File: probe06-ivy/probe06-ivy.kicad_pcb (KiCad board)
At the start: 2 copper layers, 80 x 80 mm, 106 parts, among them J1 USB_B_Micro, J2 Conn_Coaxial, Q1 S9014, SW1 SW_Push, SW2 SW_SPDT, U1 STM32F407VGTx, U2 MP1584EN, U3 AMS1117-3.3, U4 NEO-M8M, U5 XBP9B-DPST-001, U6 24LC32, U7 BMP280, Y1 8 MHz, Y2 32.768 KHz

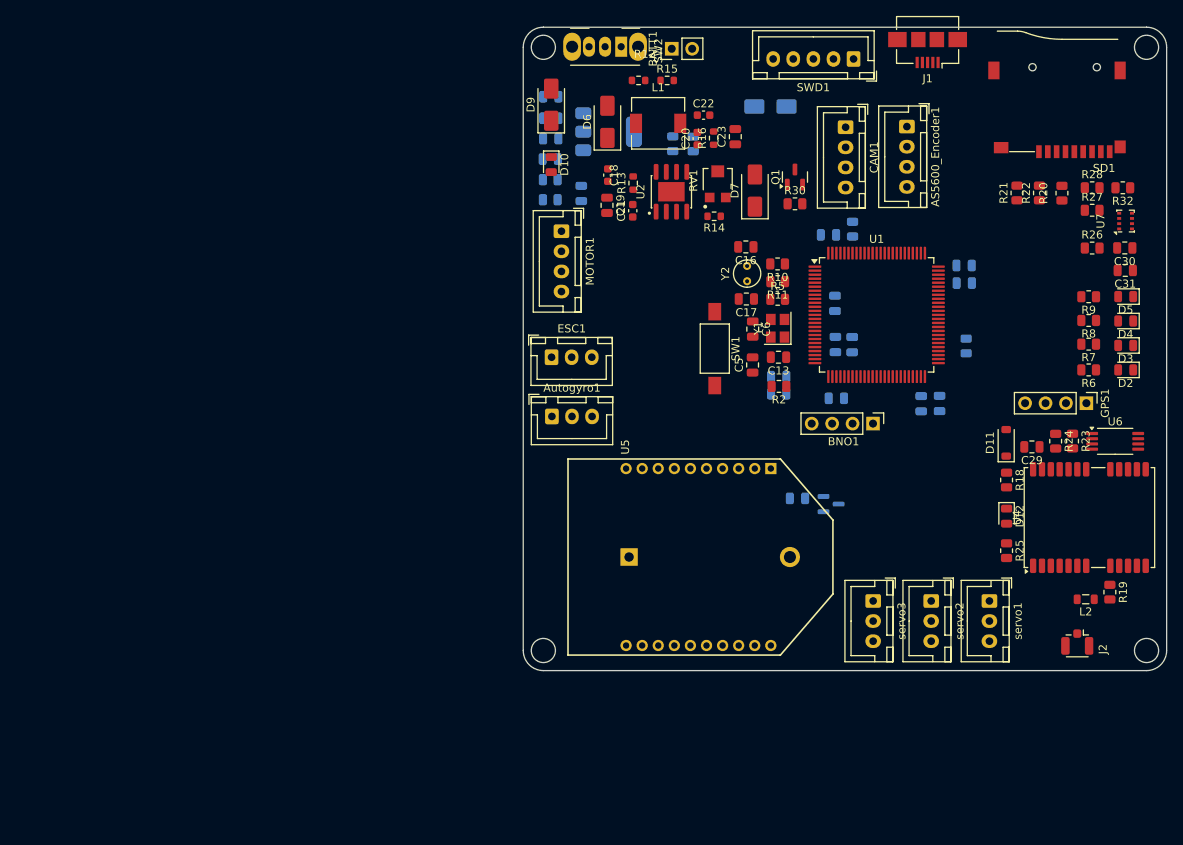
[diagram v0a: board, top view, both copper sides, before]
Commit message: route crystal and some bypass cap
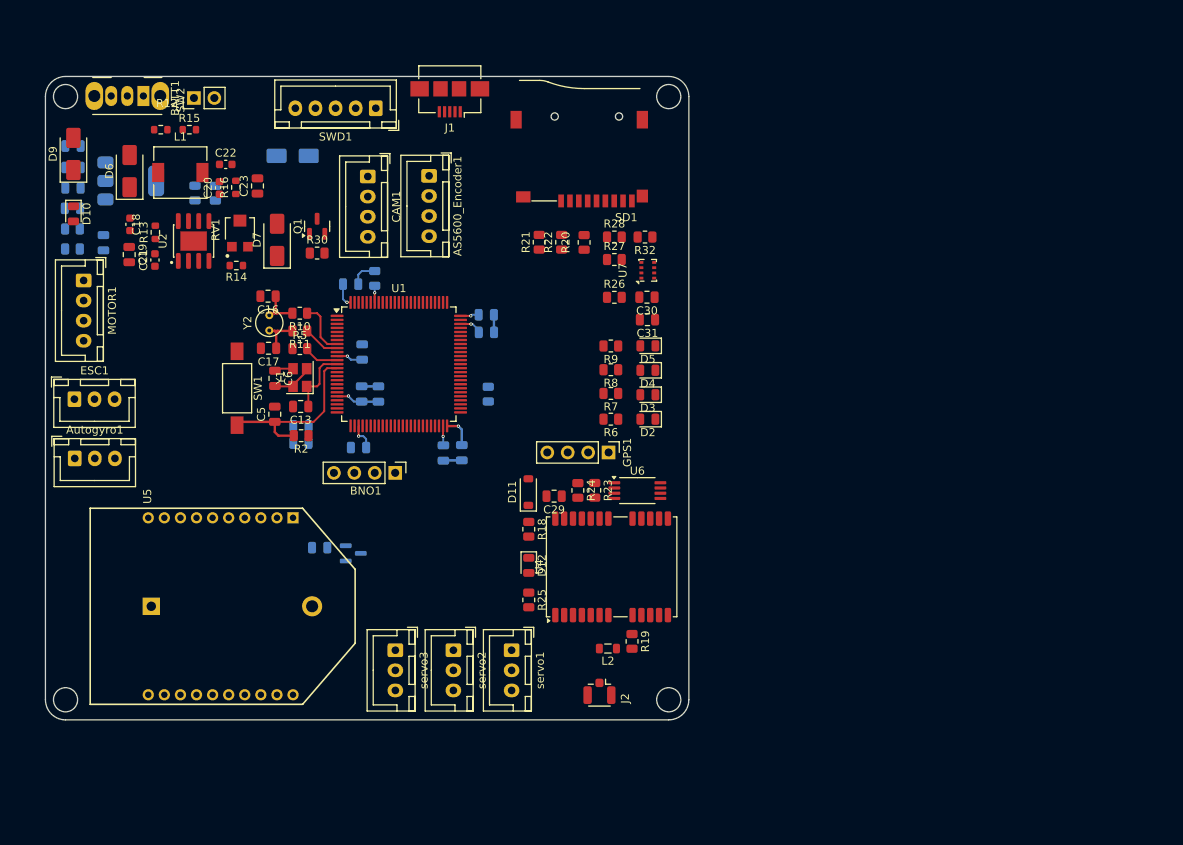
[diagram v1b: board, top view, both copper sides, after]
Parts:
- moved C10 59.7 mm to (141.5, 100.8)
- moved C11 59.7 mm to (157.4, 84.3)
- moved C24 59.7 mm to (136.7, 113.2)
- moved C3 59.7 mm to (134.4, 100.2)
- moved C30 59.7 mm to (177.4, 82.1)
- moved C4 59.7 mm to (134.4, 98.1)
- moved D2 59.7 mm to (177.5, 97.2)
- moved D3 59.7 mm to (177.5, 94.2)
- moved D5 59.7 mm to (177.5, 88.1)
- moved GPS1 59.7 mm to (172.6, 101.4)
- moved R13 59.7 mm to (116.3, 74.0)
- moved R24 59.7 mm to (168.8, 106.1)
- moved R26 59.7 mm to (173.3, 82.1)
- moved R27 59.7 mm to (173.3, 77.4)
- moved R6 59.7 mm to (172.9, 97.2)
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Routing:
- net Net-(U1-NRST): track 0.00 -> 22.4 mm
- net +3V3: track 0.00 -> 18.1 mm, vias 0 -> 5
- net GND: track 0.00 -> 17.3 mm
- net Net-(U1-PH1): track 0.00 -> 8.67 mm
- net Net-(U1-PC14): track 0.00 -> 6.81 mm
- net Net-(C16-Pad1): track 0.00 -> 5.50 mm
- net /VREF+: track 0.00 -> 5.47 mm, vias 0 -> 1
- net Net-(C17-Pad1): track 0.00 -> 5.43 mm
- net Net-(U1-PC15): track 0.00 -> 4.60 mm
- net Net-(U1-PH0): track 0.00 -> 4.44 mm
- net Net-(U1-VCAP_2): track 0.00 -> 2.85 mm, vias 0 -> 1
- net Net-(U1-VCAP_1): track 0.00 -> 2.44 mm, vias 0 -> 1
- net Net-(C6-Pad1): track 0.00 -> 2.35 mm
- net Net-(U1-BOOT0): track 0.00 -> 2.08 mm, vias 0 -> 1

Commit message: Routing (2) - make the pcb edge cuts to suit mechanic requirements - route some components (power, usb debug, gps) progress 50%
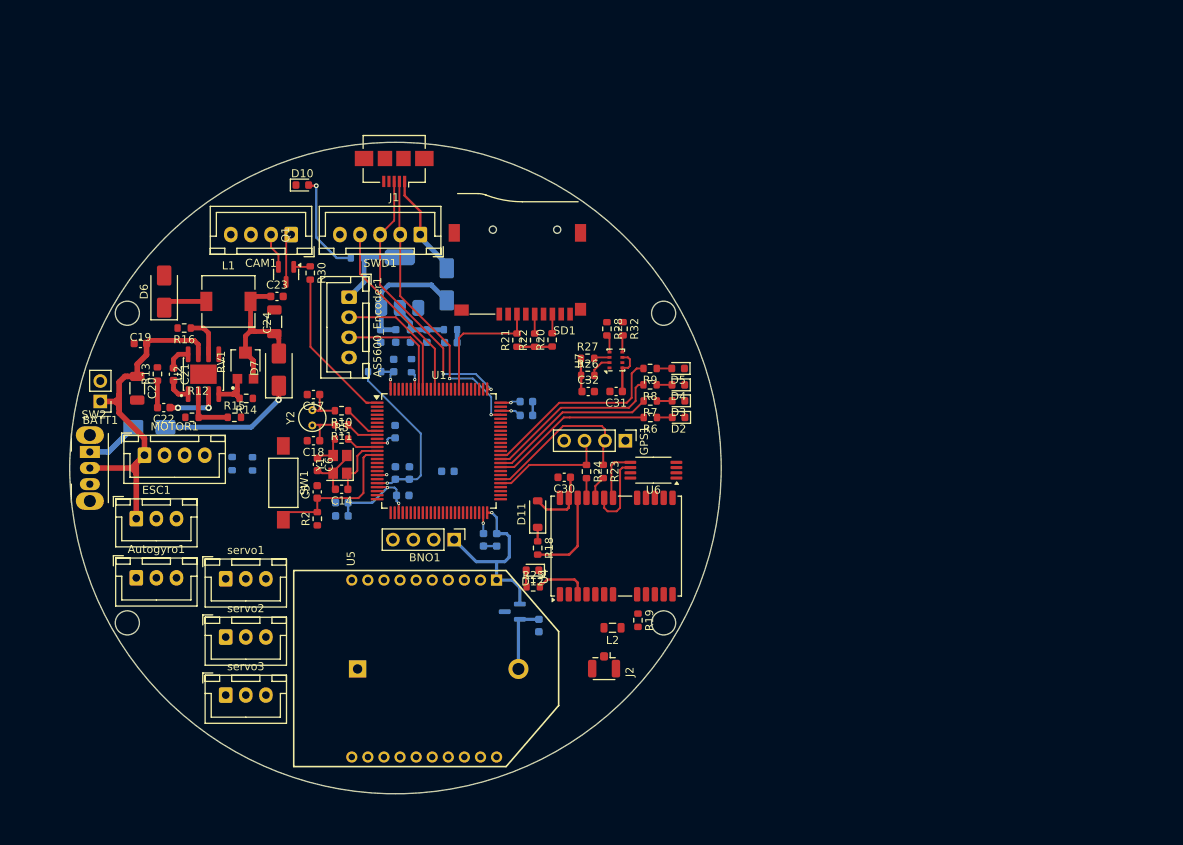
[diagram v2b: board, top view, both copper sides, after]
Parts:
- added C13: 100nF, Capacitor_SMD:C_0603_1608Metric, B.Cu at (153.0, 87.7)
- C1, C10, C11, C12, C2, C3, C4, C5, C6, C7, C8, C9: footprint Capacitor_SMD:C_0805_2012Metric -> Capacitor_SMD:C_0603_1608Metric
- C14: renamed from C13; footprint Capacitor_SMD:C_0805_2012Metric -> Capacitor_SMD:C_0603_1608Metric
- C15: renamed from C14; footprint Capacitor_SMD:C_0805_2012Metric -> Capacitor_SMD:C_0603_1608Metric
- C16: renamed from C15; footprint Capacitor_SMD:C_0805_2012Metric -> Capacitor_SMD:C_0603_1608Metric
- C17: renamed from C16; footprint Capacitor_SMD:C_0805_2012Metric -> Capacitor_SMD:C_0603_1608Metric
- C18: renamed from C17; footprint Capacitor_SMD:C_0805_2012Metric -> Capacitor_SMD:C_0603_1608Metric
- C20: renamed from C19; footprint Capacitor_SMD:C_0805_2012Metric -> Capacitor_SMD:C_1206_3216Metric
- C24: renamed from C23; footprint Capacitor_SMD:C_0805_2012Metric -> Capacitor_SMD:C_1206_3216Metric
- C25: renamed from C24; footprint Capacitor_SMD:C_0805_2012Metric -> Capacitor_SMD:C_0603_1608Metric
- C26: renamed from C25; footprint Capacitor_SMD:C_0805_2012Metric -> Capacitor_SMD:C_0603_1608Metric
- C27: renamed from C26; footprint Capacitor_SMD:C_0805_2012Metric -> Capacitor_SMD:C_0603_1608Metric
- C28: renamed from C27; footprint Capacitor_SMD:C_0805_2012Metric -> Capacitor_SMD:C_0603_1608Metric
- C29: renamed from C28; footprint Capacitor_SMD:C_0805_2012Metric -> Capacitor_SMD:C_0603_1608Metric
- C30: renamed from C29; footprint Capacitor_SMD:C_0805_2012Metric -> Capacitor_SMD:C_0603_1608Metric
- C31: renamed from C30; footprint Capacitor_SMD:C_0805_2012Metric -> Capacitor_SMD:C_0603_1608Metric
- C32: renamed from C31; footprint Capacitor_SMD:C_0805_2012Metric -> Capacitor_SMD:C_0603_1608Metric
- D10, D12, D2, D3, D4, D5: footprint LED_SMD:LED_0805_2012Metric -> LED_SMD:LED_0603_1608Metric
- D9: moved to B.Cu
- R1, R10, R11, R17, R18, R19, R2, R20, R21, R22, R23, R24, R25, R26, R27, R28, R29, R3, R30, R31, R32, R4, R5, R6, R7, R8, R9: footprint Resistor_SMD:R_0805_2012Metric -> Resistor_SMD:R_0603_1608Metric
- moved C12 51.4 mm to (152.6, 103.7), turned to 0 degrees
- moved R4 48.1 mm to (153.0, 86.1)
- moved C28 46.8 mm to (150.0, 86.9), turned to -90 degrees
- moved C29 45.8 mm to (148.0, 86.9), turned to -90 degrees
- moved C26 45.3 mm to (146.1, 86.9), turned to -90 degrees
- moved C27 45.0 mm to (144.3, 86.9), turned to -90 degrees
- moved SW2 44.8 mm to (108.1, 101.3), turned to -90 degrees
- moved BATT1 39.5 mm to (109.4, 95.0), turned to 180 degrees
- moved servo1 36.6 mm to (125.0, 117.1), turned to 0 degrees
- moved R15 36.2 mm to (126.1, 97.0)
- moved R12 36.0 mm to (120.8, 97.0)
- moved U3 35.8 mm to (146.7, 80.3), turned to 90 degrees
- moved R17 35.6 mm to (141.4, 77.2), turned to 180 degrees
- moved D9 35.3 mm to (115.5, 98.2), turned to 180 degrees
- moved R31 34.0 mm to (128.3, 102.8)
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- renumbered C18 to C19, C20 to C21, C21 to C22, C22 to C23
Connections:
- C12 pad 1: Net-(C12-Pad1) -> +3V3
- R4 pad 2: Net-(C12-Pad1) -> Net-(C13-Pad1)
- SWD1 pad 1: SWCLK -> +U5V
- SWD1 pad 3: SWO -> SWCLK
- SWD1 pad 4: +U5V -> SWO
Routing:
- net +3V3: track 18.1 -> 87.0 mm, vias 5 -> 7
- net +BATT: track 0.00 -> 46.2 mm
- net SWDIO: track 0.00 -> 36.6 mm, vias 0 -> 2
- net SWCLK: track 0.00 -> 35.9 mm, vias 0 -> 2
- net +5V: track 0.00 -> 33.2 mm, vias 0 -> 1
- net /LED4: track 0.00 -> 24.0 mm
- net SWO: track 0.00 -> 23.1 mm
- net /LED3: track 0.00 -> 22.5 mm
- net /LED2: track 0.00 -> 21.0 mm
- net Net-(D7-A): track 0.00 -> 20.5 mm
- net RX3: track 0.00 -> 20.4 mm
- net /LED1: track 0.00 -> 20.3 mm
- net +3V0: track 0.00 -> 20.0 mm
- net CAM: track 0.00 -> 19.5 mm
- net SDIO_CMD: track 0.00 -> 16.2 mm
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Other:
- board size 80 x 80 mm -> 81 x 81 mm

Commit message: Routing (3) Signal routing mostly done with something that needs TODO next: - Correction for power signals - Tidy up component silkscreen - Add team name and tagline
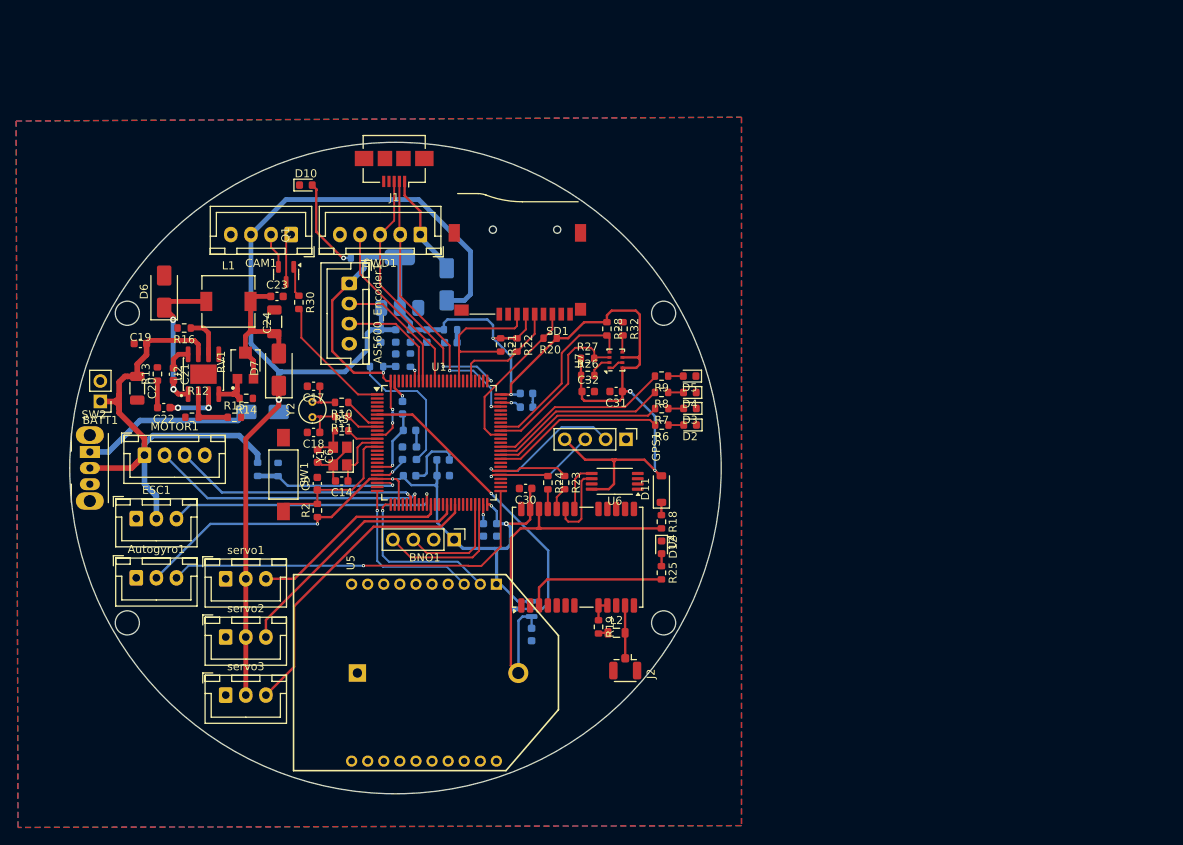
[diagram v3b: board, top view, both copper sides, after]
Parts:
- moved D12 16.3 mm to (179.2, 113.2), turned to -90 degrees
- moved R25 16.0 mm to (179.2, 116.3), turned to -90 degrees
- moved R18 15.7 mm to (179.2, 110.0)
- moved D11 15.7 mm to (179.2, 105.9)
- moved D9 14.2 mm to (129.6, 96.3)
- moved C4 13.0 mm to (152.1, 104.3), turned to 180 degrees
- moved C3 9.80 mm to (147.9, 104.3), turned to 180 degrees
- moved C12 6.97 mm to (147.9, 98.6)
- moved C10 6.68 mm to (152.0, 102.3)
- moved R23 5.00 mm to (167.1, 105.1)
- moved R24 5.00 mm to (165.1, 105.1)
- moved U4 5.00 mm to (168.8, 114.4)
- moved U6 5.00 mm to (173.4, 105.0)
- moved C30 5.00 mm to (162.3, 105.8)
- moved R19 4.97 mm to (171.4, 123.1)
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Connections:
- Autogyro1 pad 1: Autogyro -> GND
- Autogyro1 pad 3: GND -> Autogyro
- ESC1 pad 1: +BATT -> GND
- ESC1 pad 2: PWM1 -> +BATT
- ESC1 pad 3: GND -> PWM3
- MOTOR1 pad 2: PWM6 -> PWM2
- MOTOR1 pad 3: PWM5 -> PWM1
- U1 pad 18: Autogyro -> unconnected-(U1-PC3-Pad18)
- U1 pad 51: unconnected-(U1-PB12-Pad51) -> Autogyro
- servo1 pad 1: PWM2 -> GND
- servo1 pad 3: GND -> PWM4
- servo2 pad 1: PWM3 -> GND
- servo2 pad 3: GND -> PWM5
- servo3 pad 1: PWM4 -> GND
- servo3 pad 3: GND -> PWM6
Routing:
- net +3V3: track 87.0 -> 256.2 mm, vias 7 -> 12
- net +5V: track 33.2 -> 126.3 mm
- net Autogyro: track 0.00 -> 48.9 mm, vias 0 -> 1
- net /VBAT: track 0.00 -> 39.0 mm, vias 0 -> 1
- net PWM6: track 0.00 -> 38.4 mm
- net PWM2: track 0.00 -> 34.8 mm, vias 0 -> 1
- net PWM3: track 0.00 -> 34.3 mm, vias 0 -> 1
- net PWM5: track 0.00 -> 31.3 mm
- net PWM1: track 0.00 -> 31.2 mm, vias 0 -> 1
- net +3V0: track 20.0 -> 49.0 mm
- net PWM4: track 0.00 -> 25.0 mm
- net RX2: track 0.00 -> 20.8 mm, vias 0 -> 1
- net TX2: track 0.00 -> 20.7 mm, vias 0 -> 1
- net SCL3: track 2.21 -> 22.3 mm
- net VOLT: track 0.00 -> 19.3 mm, vias 0 -> 1
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- added copper zone on B.Cu, net GND
- added copper zone on F.Cu, net GND

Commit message: Routing (3)
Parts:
- added G***: LOGO, graphics:logobamantara, B.Cu at (164.0, 83.0)
- SD CARD: renamed from SD1
- U-BLOX: renamed from U4; value NEO-M8M -> U-BLOX
- moved C30 1.82 mm to (163.3, 104.4)
- moved D11 1.62 mm to (179.7, 104.4)
- moved D12 1.62 mm to (179.8, 111.6)
- moved J2 1.62 mm to (175.2, 126.5)
- moved R18 1.62 mm to (179.7, 108.5)
- moved R24 1.62 mm to (165.6, 103.6)
- moved R25 1.62 mm to (179.7, 114.8)
- moved U-BLOX 1.62 mm to (169.3, 112.9)
- moved U6 1.62 mm to (173.9, 103.4)
- moved R23 1.62 mm to (167.7, 103.6)
- moved R19 1.62 mm to (171.9, 121.5)
- moved L2 1.56 mm to (174.2, 122.3)
- moved D2 1.31 mm to (182.7, 99.3)
- moved R6 1.30 mm to (179.3, 99.3)
- moved D3 0.79 mm to (182.7, 96.7)
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- renumbered AS5600_Encoder1 to AS5600, Autogyro1 to Autogyro, U7 to BMP280, BNO1 to BNO055, GPS1 to GPS, SWD1 to SWD, U5 to XBEE
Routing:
- net GND: track 23.0 -> 33.5 mm, vias 1 -> 59
- net +BATT: track 64.8 -> 72.1 mm
- net +3V0: track 49.0 -> 44.4 mm
- net /VBAT: track 39.0 -> 35.0 mm
- net +3V3: track 256.2 -> 252.8 mm
- net Net-(D2-A): track 1.90 -> 0.00 mm
- net Net-(D3-A): track 1.90 -> 0.00 mm
- net TX3: track 21.0 -> 22.3 mm
- net Net-(U1-VCAP_1): track 3.44 -> 2.42 mm
- net Net-(D7-A): track 20.5 -> 19.7 mm
- net RX3: track 27.9 -> 28.7 mm
- net Net-(D6-K): track 19.4 -> 20.0 mm
- net /LED1: track 21.5 -> 22.1 mm
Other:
- board text added: "#3121 Bamantara EEPISAT"
- board text added: "#DOA_IBU #Bismillah_Juara_1"
- board text added: "+"
- board text added: "-"
- board text added: "CanSat Competition 2025 Auto Gyro Descender"
- board text added: "Garudaku Jaya Diangkasa"
- board text added: "RX"
- board text added: "S"
- board text added: "TX"

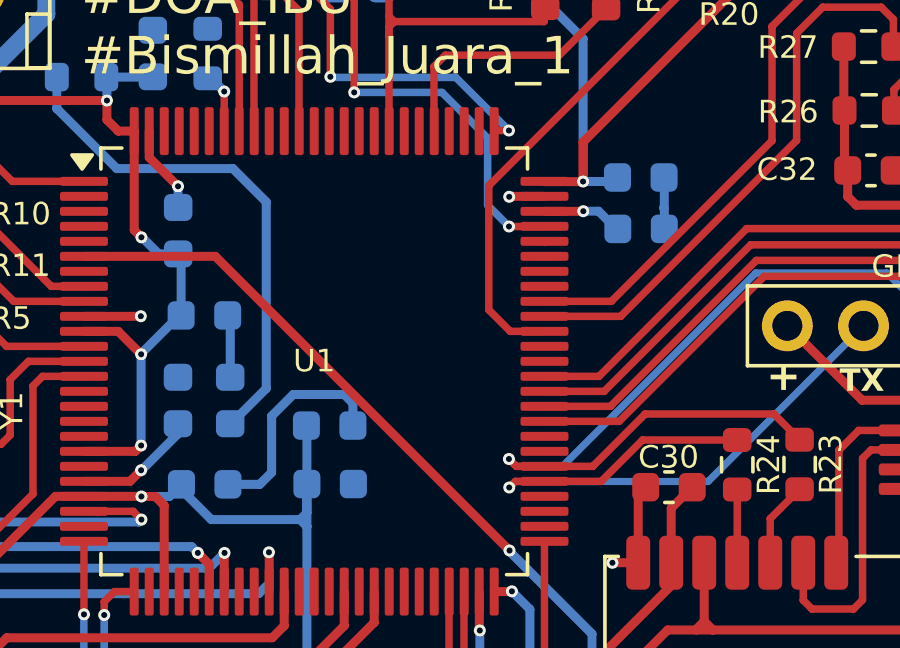
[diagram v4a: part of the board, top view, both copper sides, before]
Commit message: order id placement
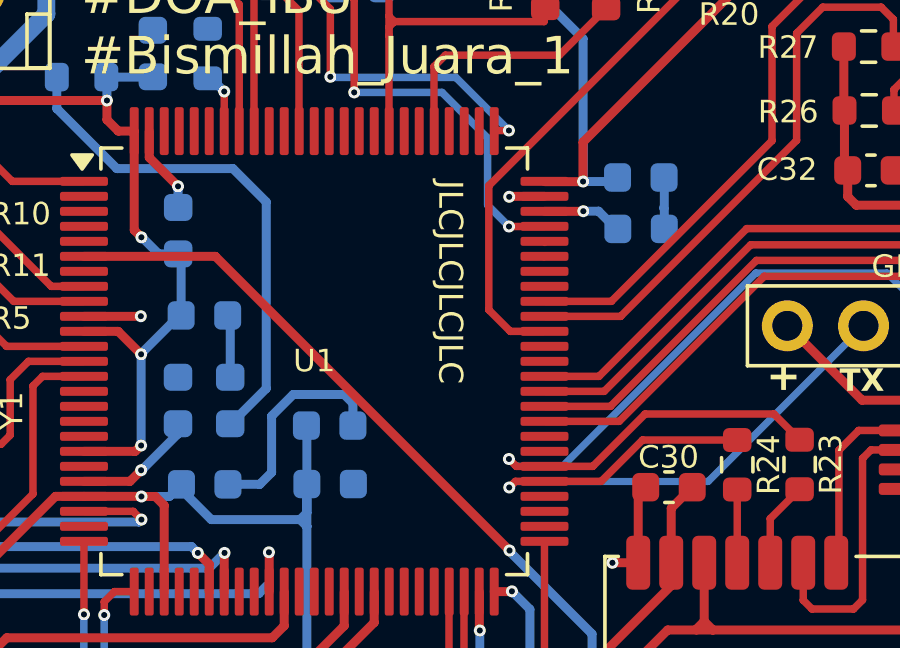
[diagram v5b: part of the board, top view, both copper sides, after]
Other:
- board text added: "JLCJLCJLCJLC"
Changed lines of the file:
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@@
 			(plot_on_all_layers_selection 0x0000000_00000000)
 			(disableapertmacros no)
-			(usegerberextensions no)
-			(usegerberattributes yes)
-			(usegerberadvancedattributes yes)
-			(creategerberjobfile yes)
+			(usegerberextensions yes)
+			(usegerberattributes no)
+			(usegerberadvancedattributes no)
+			(creategerberjobfile no)
 			(dashed_line_dash_ratio 12.000000)
 			(dashed_line_gap_ratio 3.000000)
@@
 			(psa4output no)
 			(plotreference yes)
-			(plotvalue yes)
+			(plotvalue no)
 			(plotfptext yes)
 			(plotinvisibletext no)
 			(sketchpadsonfab no)
-			(subtractmaskfromsilk no)
+			(subtractmaskfromsilk yes)
 			(outputformat 1)
 			(mirror no)
-			(drillshape 1)
+			(drillshape 0)
 			(scaleselection 1)
-			(outputdirectory "")
+			(outputdirectory "gerber/")
 		)
 	)
@@
 		(fp_arc
 			(start 6.1679 9.656)
-			(mid 5.659554 9.609621)
+			(mid 5.659557 9.609613)
 			(end 5.168 9.472)
 			(stroke
@@
 			)
 			(justify left bottom)
+		)
+	)
+	(gr_text "JLCJLCJLCJLC"
+		(at 155.59 94.12 270)
+		(layer "F.SilkS")
+		(effects
+			(font
+				(size 0.8 0.8)
+				(thickness 0.15)
+			)
+			(justify left bottom)
